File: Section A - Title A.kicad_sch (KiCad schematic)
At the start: 0 parts

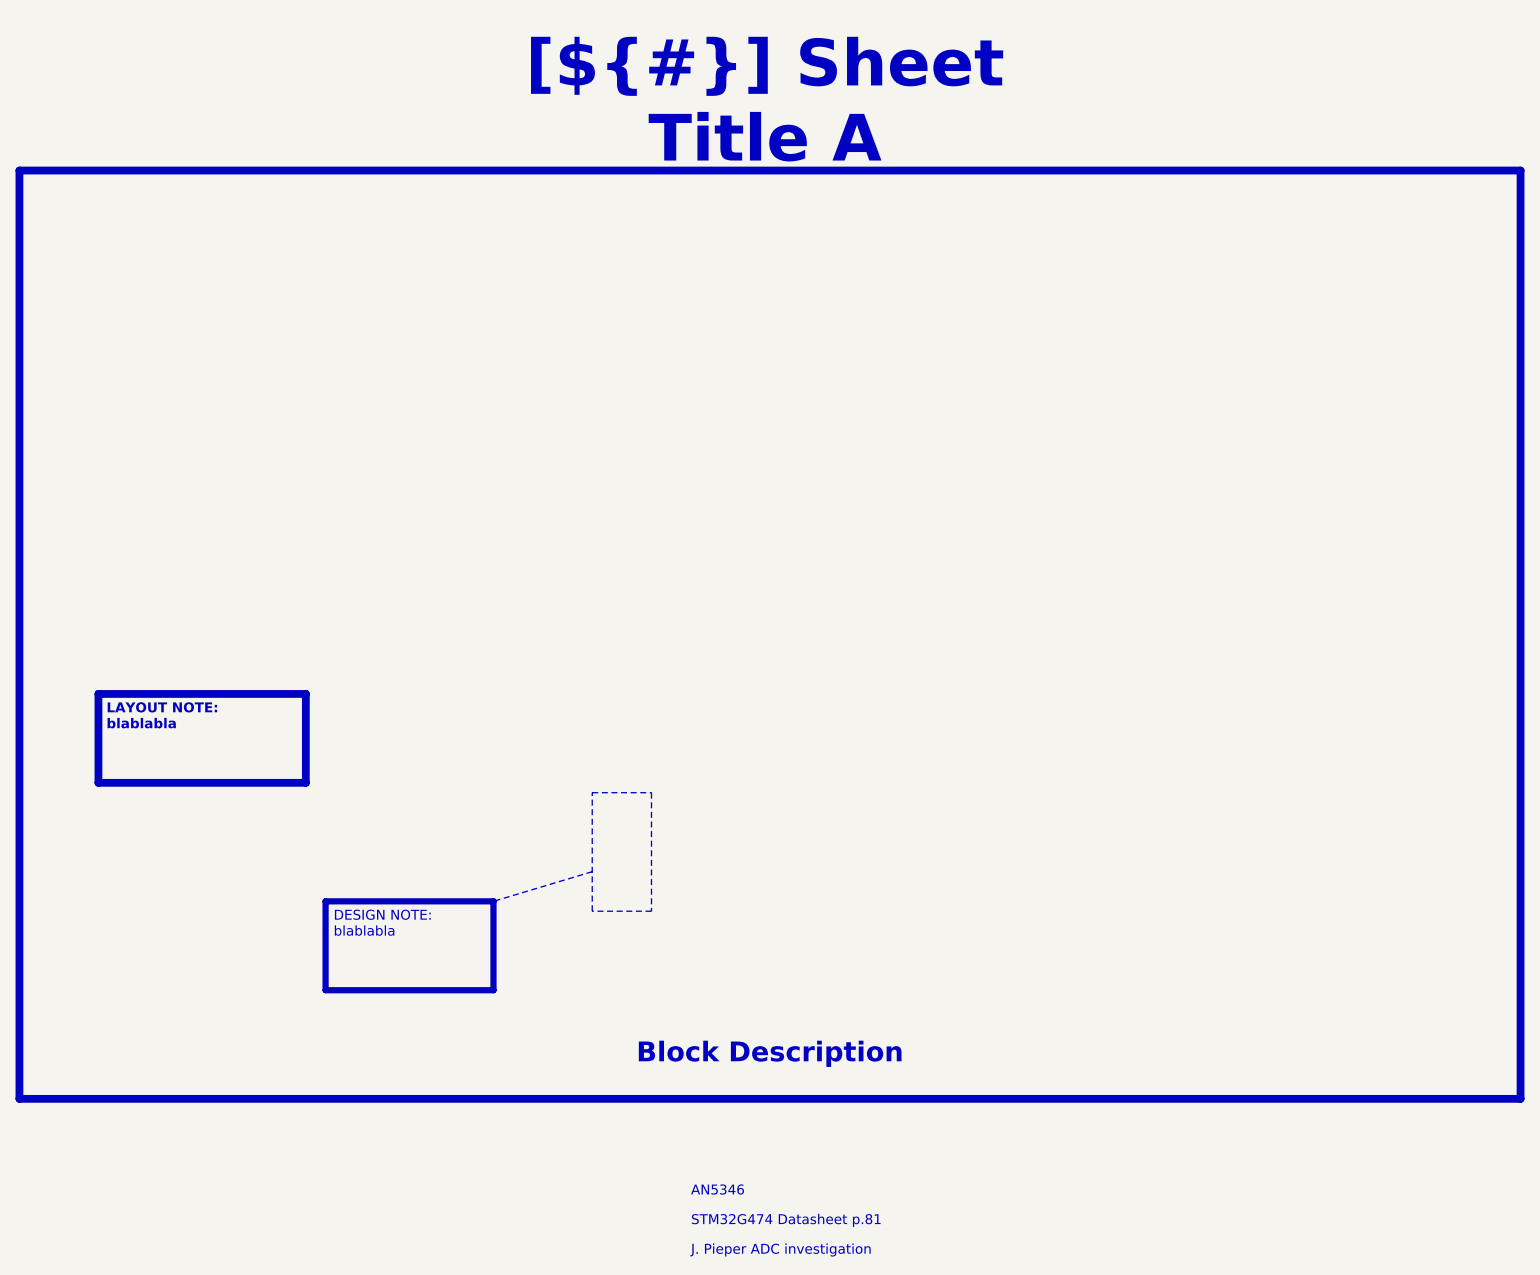
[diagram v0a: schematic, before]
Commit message: [Schematics] Merging changes from the initial project to the Template
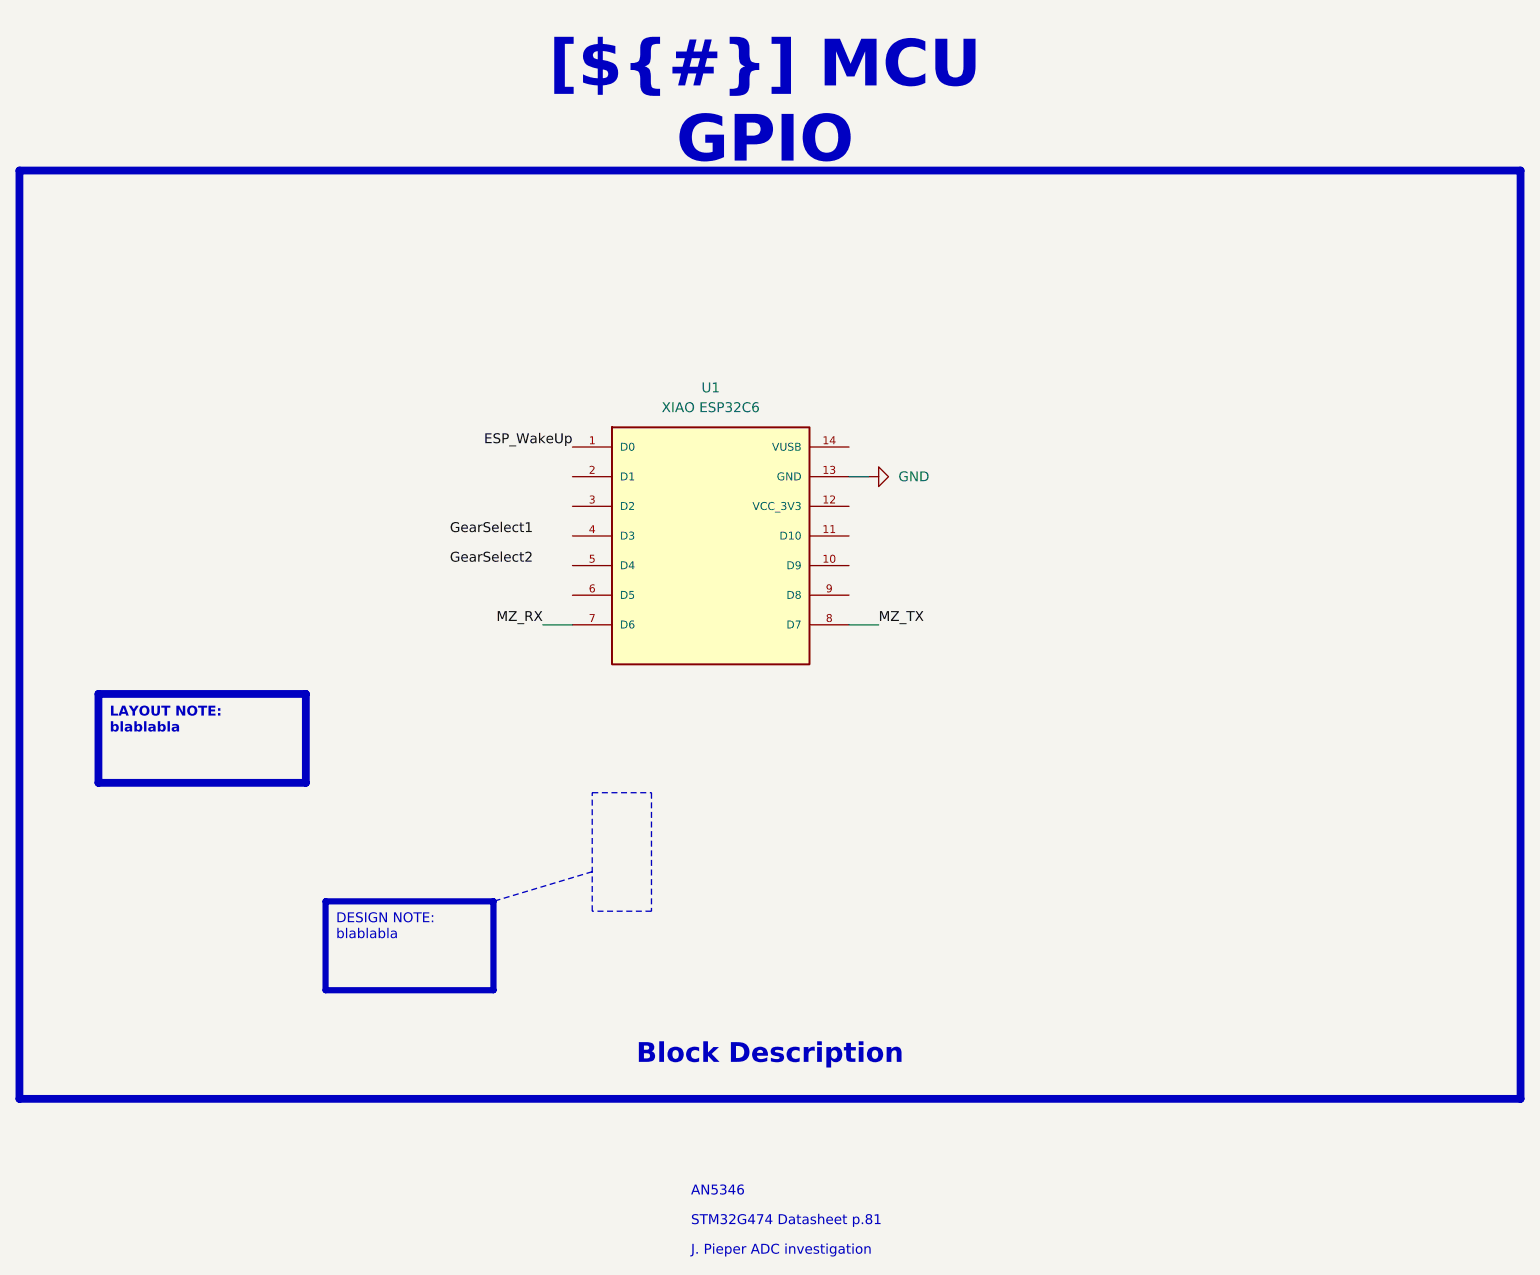
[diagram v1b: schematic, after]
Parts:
- added U1: XIAO ESP32C6, LEGACY:XIAO-ESP32C6-DIP, symbol Legacy:XIAO_ESP32C3
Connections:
- new net ESP_WakeUp: U1.1 (D0)
- new net GND: U1.13 (GND)
- new net MZ_RX: U1.7 (D6)
- new net MZ_TX: U1.8 (D7)
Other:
- title: Sheet Title A -> MCU GPIO
